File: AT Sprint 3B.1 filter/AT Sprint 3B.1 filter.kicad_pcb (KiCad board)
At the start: 2 copper layers, 53.4 x 22.2 mm, 18 parts

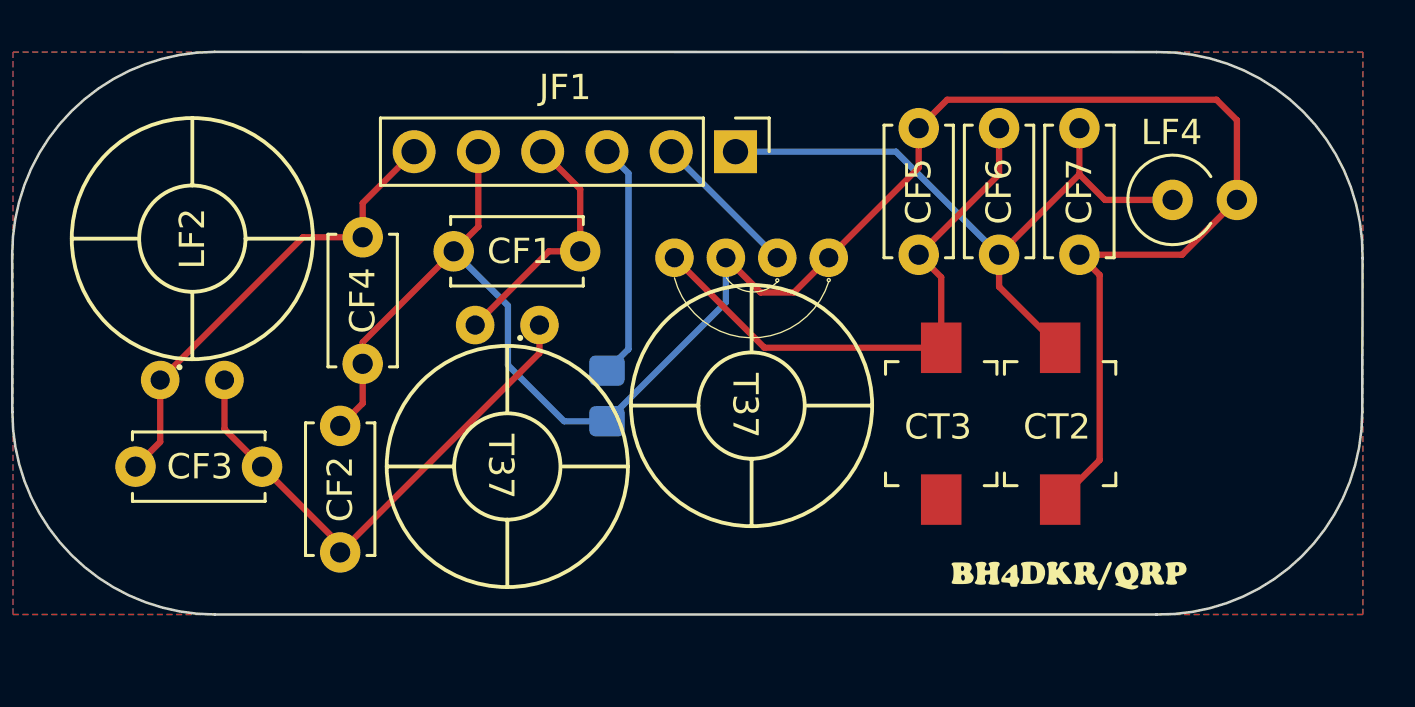
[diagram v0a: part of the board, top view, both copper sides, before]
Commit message: add filter boundary in User.Drawing layer, fit room for filter board
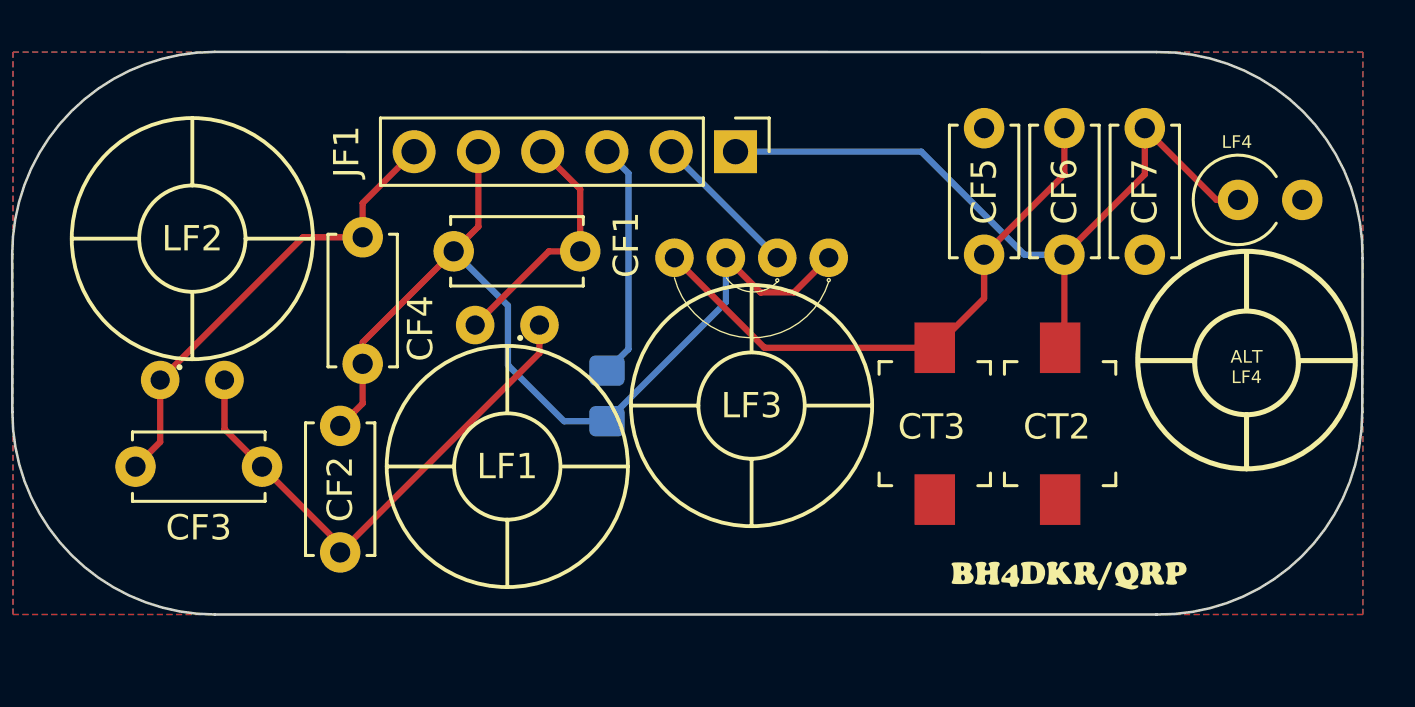
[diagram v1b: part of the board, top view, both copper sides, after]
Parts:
- added G***: LOGO, CraftsmanICs:arrow_up, B.Cu at (112.6, 49.5)
- added G***: LOGO, CraftsmanICs:arrow_up, B.Cu at (118.0, 49.5)
- added G***: LOGO, CraftsmanICs:arrow_up, B.Cu at (108.1, 49.5)
- added G***: LOGO, CraftsmanICs:arrow_up, B.Cu at (113.3, 49.5)
- added G***: LOGO, CraftsmanICs:arrow_up, B.Cu at (107.6, 49.5)
- added G***: LOGO, CraftsmanICs:arrow_up, B.Cu at (120.5, 49.5)
- moved CF5 2.58 mm to (130.3, 55.6)
- moved CF7 2.58 mm to (136.7, 55.6)
- moved LF4 2.58 mm to (140.4, 53.5)
- moved CF6 2.58 mm to (133.5, 50.6)
- moved CT3 0.25 mm to (128.4, 62.3)
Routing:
- net GNDREF: track 77.8 -> 36.9 mm
- net Net-(CF6-Pad2): track 27.2 -> 29.8 mm
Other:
- board text added: "ALT LF4"
- board text added: "ANT"
- board text added: "BPF"
- board text added: "GND"
- board text added: "LPF"
- board text added: "RX"
- board text added: "TX"

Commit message: generate ats3b1 filter gerb file
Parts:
- removed the G*** at (133.7, 68.3)
- CT2, CT3: footprint Capacitor_SMD:C_Trimmer_Murata_TZB4-B -> CraftsmanICs:C_TRIMMER_TZ03
- moved G*** 19.8 mm to (94.1, 58.4), turned to -90 degrees
- moved G*** 12.2 mm to (119.3, 66.4)
- moved CT3 2.75 mm to (129.8, 59.9), turned to 180 degrees
- moved CT2 2.58 mm to (134.1, 64.8), turned to 0 degrees
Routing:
- net GNDREF: track 36.9 -> 49.4 mm
- net Net-(CF6-Pad2): track 29.8 -> 36.3 mm
- net Net-(CF5-Pad1): track 22.6 -> 24.5 mm
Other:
- board text added: "15"
- board text added: "17"
- board text added: "20"
- board text added: "30"
- board text added: "40"
- board text added: "80"
- board text added: "BAND SEL"
- board text removed: "15m"
- board text removed: "17m"
- board text removed: "20m"
- board text removed: "30m"
- board text removed: "40m"
- board text removed: "80m"

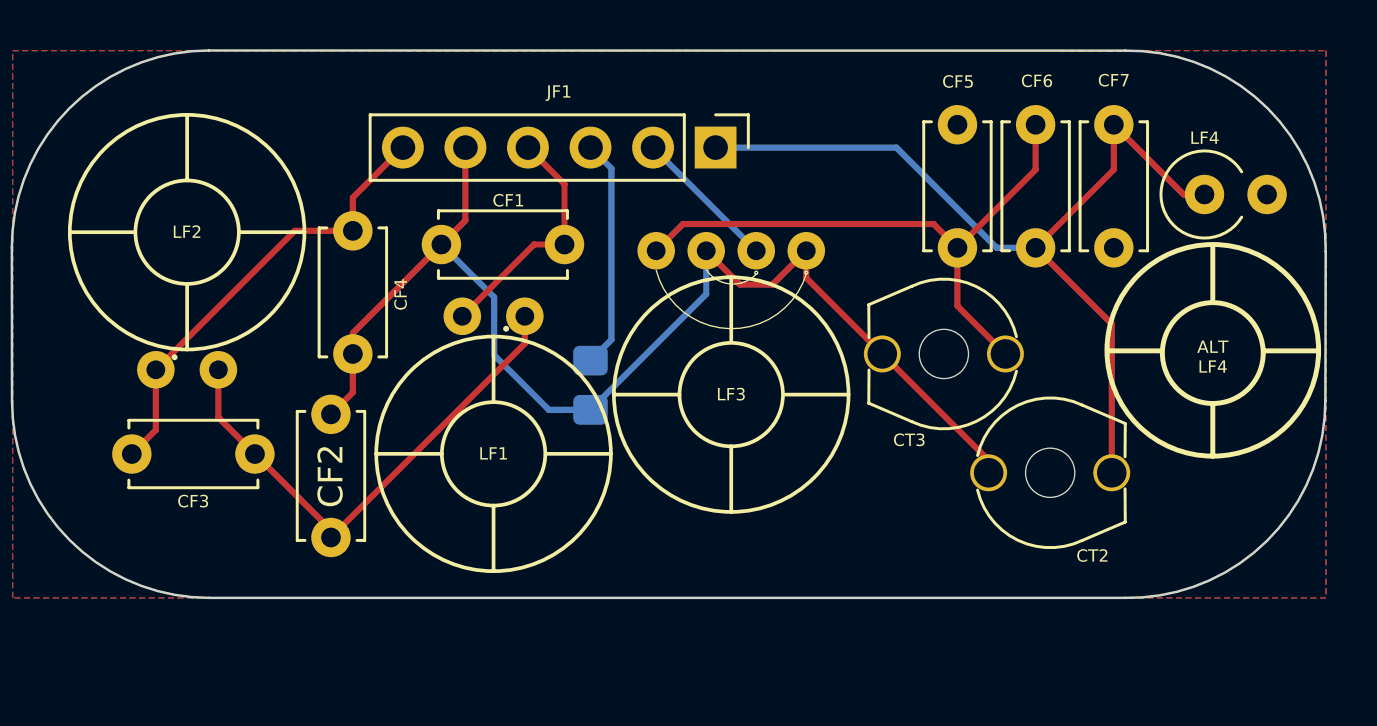
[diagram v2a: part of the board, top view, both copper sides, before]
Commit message: change text size for production
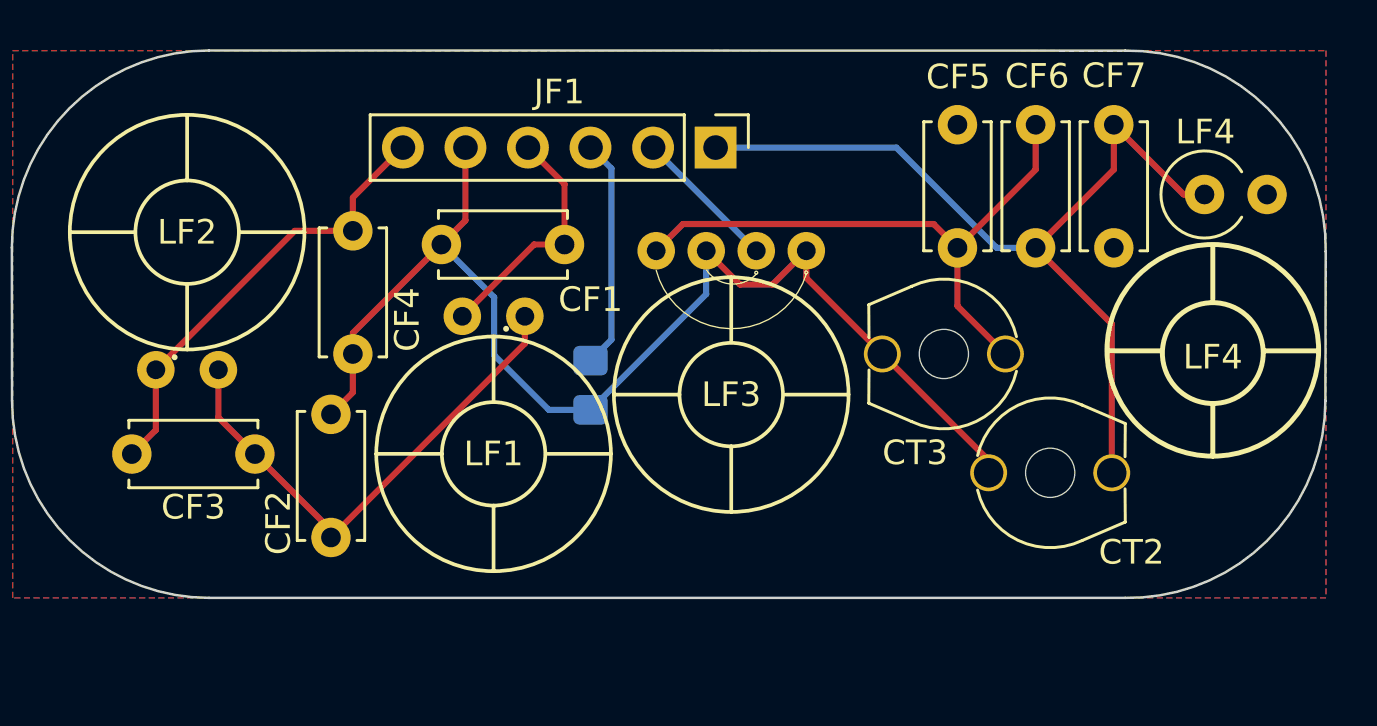
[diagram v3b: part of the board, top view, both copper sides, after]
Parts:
- moved G*** 0.18 mm to (112.6, 49.7)
- moved G*** 0.18 mm to (118.0, 49.7)
- moved G*** 0.18 mm to (113.3, 49.7)
- moved G*** 0.15 mm to (108.1, 49.7)
- moved G*** 0.15 mm to (107.6, 49.7)
- moved G*** 0.15 mm to (120.5, 49.7)
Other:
- board text added: "LF4"
- board text removed: "ALT LF4"
- board text removed: "BAND SEL"
